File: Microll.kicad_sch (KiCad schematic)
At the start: 6 parts, among them J1 USB_C_Receptacle, U1 AP7173-FNG-7, U2 STM32G0B1CBU6, U3 ESP32-C3-WROOM-02-N4, U4 LSM6DSL

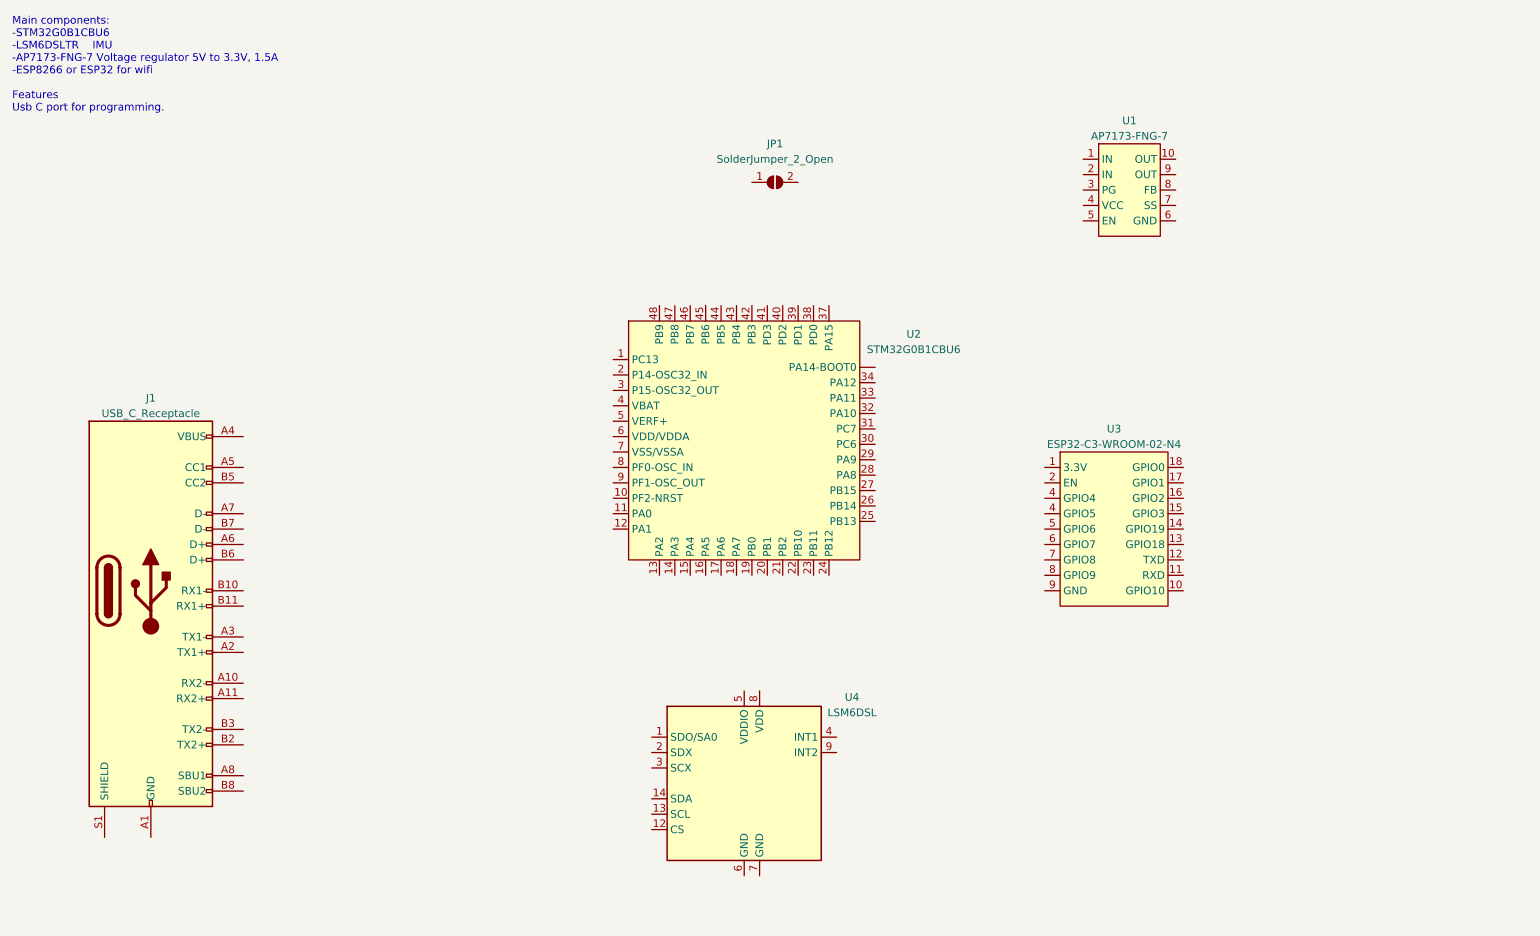
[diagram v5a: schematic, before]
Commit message: Added some notes on programming the STM32 and ESP32 over USB. Added datasheets to all components.
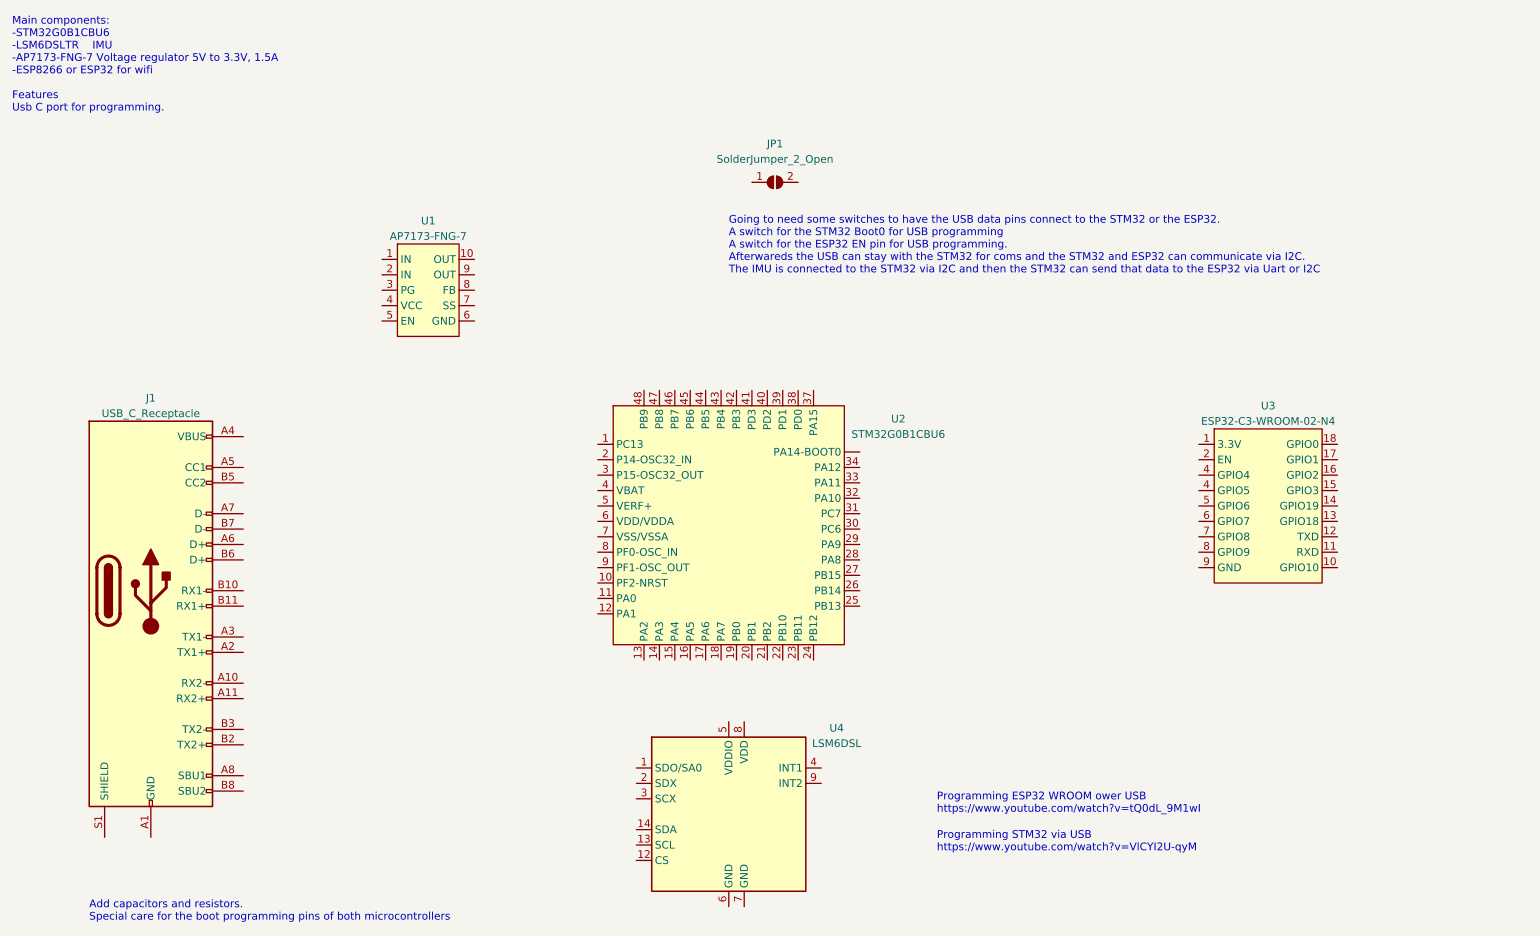
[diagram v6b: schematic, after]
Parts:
- J1: Datasheet2 (none) -> https://mm.digikey.com/Volume0/opasdata/d220001/medias/docu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
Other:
- note added: "Add capacitors and resistors. Special care for the boot programming pins of both microcontrollers"
- note added: "Going to need some switches to have the USB data pins connect to the STM32 or the ESP32. A switch for the STM32 Boot0 for USB programming A switch for the ESP32 EN pin for USB programming. Afterwareds the USB can stay with the STM32 for coms and the STM32 and ESP32 can communicate via I2C. The IMU is connected to the STM32 via I2C and then the STM32 can send that data to the ESP32 via Uart or I2C"
- note added: "Programming ESP32 WROOM ower USB https://www.youtube.com/watch?v=tQ0dL_9M1wI"
- note added: "Programming STM32 via USB https://www.youtube.com/watch?v=VlCYI2U-qyM"
- moved on the sheet: U1, U2, U3, U4
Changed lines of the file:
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@@
 (kicad_sch (version 20211123) (generator eeschema)
   (paper "A4")
+  (text "Going to need some switches to have the USB data pins connect to the STM32 or the ESP32.\nA switch for the STM32 Boot0 for USB programming\nA switch for the ESP32 EN pin for USB programming.\nAfterwareds the USB can stay with the STM32 for coms and the STM32 and ESP32 can communicate via I2C.\nThe IMU is connected to the STM32 via I2C and then the STM32 can send that data to the ESP32 via Uart or I2C"
+    (at 133.35 58.42 0)
+    (effects (font (size 1.27 1.27)) (justify left bottom))
+  )
+  (text "Programming ESP32 WROOM ower USB\nhttps://www.youtube.com/watch?v=tQ0dL_9M1wI"
+    (at 167.64 147.32 0)
+    (effects (font (size 1.27 1.27)) (justify left bottom))
+  )
+  (text "Programming STM32 via USB\nhttps://www.youtube.com/watch?v=VlCYI2U-qyM"
+    (at 167.64 153.67 0)
+    (effects (font (size 1.27 1.27)) (justify left bottom))
+  )
+  (text "Add capacitors and resistors.\nSpecial care for the boot programming pins of both microcontrollers"
+    (at 27.94 165.1 0)
+    (effects (font (size 1.27 1.27)) (justify left bottom))
+  )
   (text "Main components:\n-STM32G0B1CBU6	\n-LSM6DSLTR	IMU\n-AP7173-FNG-7 Voltage regulator 5V to 3.3V, 1.5A\n-ESP8266 or ESP32 for wifi\n\nFeatures\nUsb C port for programming."
     (at 15.24 31.75 0)
@@
     (pin "2")
   )
-  (symbol (lib_id "ESP32:ESP32-C3-WROOM-02-N4") (at 196.85 96.52 0) (unit 1)
+  (symbol (lib_id "ESP32:ESP32-C3-WROOM-02-N4") (at 222.25 92.71 0) (unit 1)
     (in_bom yes) (on_board yes)
-    (property "Reference" "U3" (id 0) (at 196.85 83.82 0))
-    (property "Value" "ESP32-C3-WROOM-02-N4" (id 1) (at 196.85 86.36 0))
-    (property "Footprint" "ESP32:ESP32-C3-WROOM-02-N4" (id 2) (at 196.85 96.52 0)
+    (property "Reference" "U3" (id 0) (at 222.25 80.01 0))
+    (property "Value" "ESP32-C3-WROOM-02-N4" (id 1) (at 222.25 82.55 0))
+    (property "Footprint" "ESP32:ESP32-C3-WROOM-02-N4" (id 2) (at 222.25 92.71 0)
       (effects (font (size 1.27 1.27)) hide)
     )
-    (property "Datasheet" "" (id 3) (at 196.85 96.52 0)
+    (property "Datasheet" "https://www.espressif.com/sites/default/files/documentation/esp32-c3-wroom-02_datasheet_en.pdf" (id 3) (at 222.25 92.71 0)
       (effects (font (size 1.27 1.27)) hide)
     )
@@
     (pin "9")
   )
-  (symbol (lib_id "STM32:STM32G0B1CBU6") (at 135.89 86.36 0) (unit 1)
+  (symbol (lib_id "STM32:STM32G0B1CBU6") (at 133.35 100.33 0) (unit 1)
     (in_bom yes) (on_board yes) (fields_autoplaced)
-    (property "Reference" "U2" (id 0) (at 163.83 68.1988 0))
-    (property "Value" "STM32G0B1CBU6" (id 1) (at 163.83 70.7388 0))
-    (property "Footprint" "STM32:STM32G0B1CBU6" (id 2) (at 128.27 77.47 0)
+    (property "Reference" "U2" (id 0) (at 161.29 82.1688 0))
+    (property "Value" "STM32G0B1CBU6" (id 1) (at 161.29 84.7088 0))
+    (property "Footprint" "STM32:STM32G0B1CBU6" (id 2) (at 125.73 91.44 0)
       (effects (font (size 1.27 1.27)) hide)
     )
-    (property "Datasheet" "" (id 3) (at 128.27 77.47 0)
+    (property "Datasheet" "file:///home/ruben/Downloads/stm32g0b1cb.pdf" (id 3) (at 125.73 91.44 0)
       (effects (font (size 1.27 1.27)) hide)
     )
@@
     (pin "9")
   )
-  (symbol (lib_id "AP7173-FNG-7:AP7173-FNG-7") (at 199.39 41.91 0) (unit 1)
+  (symbol (lib_id "AP7173-FNG-7:AP7173-FNG-7") (at 83.82 58.42 0) (unit 1)
     (in_bom yes) (on_board yes)
-    (property "Reference" "U1" (id 0) (at 199.39 33.02 0))
-    (property "Value" "AP7173-FNG-7" (id 1) (at 199.39 35.56 0))
-    (property "Footprint" "AP7173-FNG-7:AP7173-FNG-7" (id 2) (at 198.12 41.91 0)
+    (property "Reference" "U1" (id 0) (at 83.82 49.53 0))
+    (property "Value" "AP7173-FNG-7" (id 1) (at 83.82 52.07 0))
+    (property "Footprint" "AP7173-FNG-7:AP7173-FNG-7" (id 2) (at 82.55 58.42 0)
       (effects (font (size 1.27 1.27)) hide)
     )
-    (property "Datasheet" "" (id 3) (at 198.12 41.91 0)
+    (property "Datasheet" "https://www.diodes.com/assets/Datasheets/AP7173.pdf" (id 3) (at 82.55 58.42 0)
       (effects (font (size 1.27 1.27)) hide)
     )
@@
     (pin "9")
   )
-  (symbol (lib_id "Sensor_Motion:LSM6DSL") (at 135.89 142.24 0) (unit 1)
+  (symbol (lib_id "Sensor_Motion:LSM6DSL") (at 133.35 147.32 0) (unit 1)
     (in_bom yes) (on_board yes) (fields_autoplaced)
-    (property "Reference" "U4" (id 0) (at 153.67 128.0412 0))
-    (property "Value" "LSM6DSL" (id 1) (at 153.67 130.5812 0))
-    (property "Footprint" "Package_LGA:LGA-14_3x2.5mm_P0.5mm_LayoutBorder3x4y" (id 2) (at 125.73 160.02 0)
+    (property "Reference" "U4" (id 0) (at 151.13 133.1212 0))
+    (property "Value" "LSM6DSL" (id 1) (at 151.13 135.6612 0))
+    (property "Footprint" "Package_LGA:LGA-14_3x2.5mm_P0.5mm_LayoutBorder3x4y" (id 2) (at 123.19 165.1 0)
       (effects (font (size 1.27 1.27)) (justify left) hide)
     )
-    (property "Datasheet" "https://www.st.com/resource/en/datasheet/lsm6dsl.pdf" (id 3) (at 138.43 158.75 0)
+    (property "Datasheet" "https://www.st.com/resource/en/datasheet/lsm6dsl.pdf" (id 3) (at 135.89 163.83 0)
       (effects (font (size 1.27 1.27)) hide)
     )
@@
       (effects (font (size 1.27 1.27)) hide)
     )
+    (property "Datasheet2" "https://mm.digikey.com/Volume0/opasdata/d220001/medias/docus/5492/USB4105.pdf" (id 4) (at 38.1 110.49 0)
+      (effects (font (size 1.27 1.27)) hide)
+    )

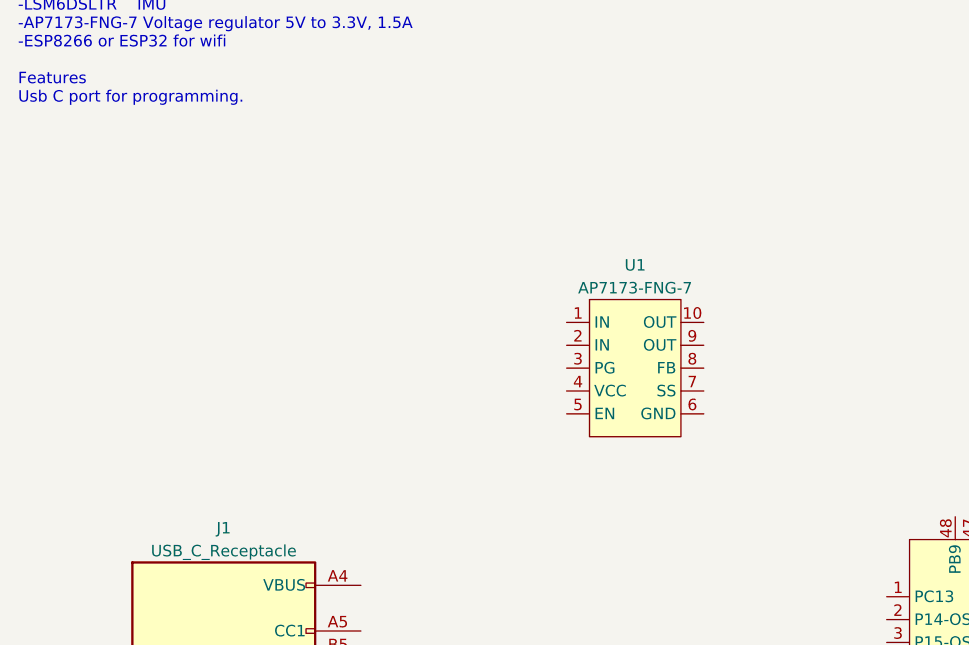
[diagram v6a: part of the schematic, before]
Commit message: Begun drafting linear regulator circuit and passive components
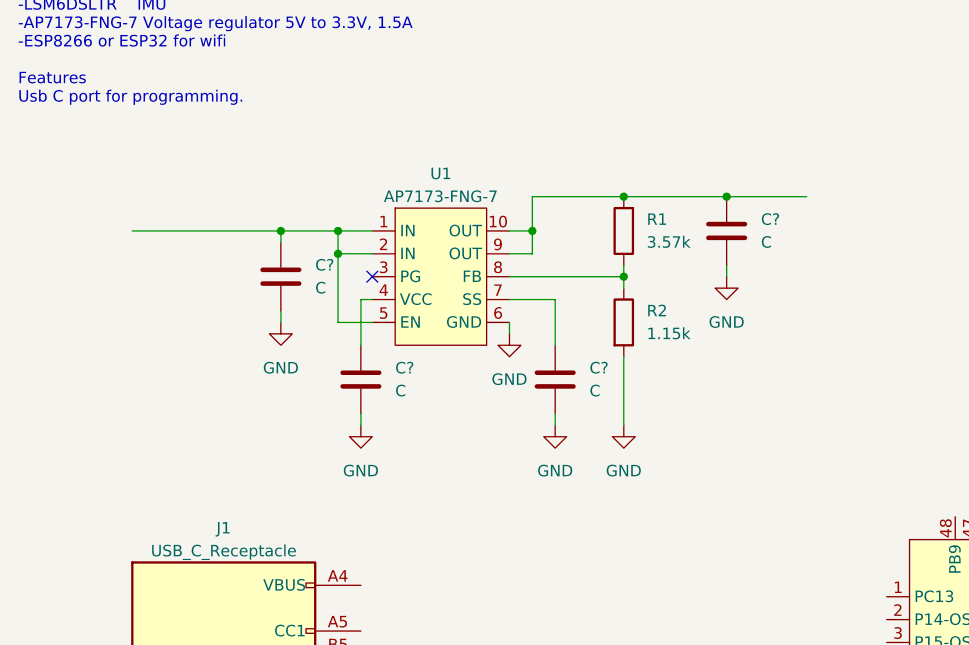
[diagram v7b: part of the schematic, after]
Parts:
- added C? (x4): C, symbol Device:C
- added R1: 3.57k, symbol Device:R
- added R2: 1.15k, symbol Device:R
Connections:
- net at U1.1 (IN): now also U1.2 (IN), U1.5 (EN), C?.1
- net at U1.10 (OUT): now also U1.9 (OUT), C?.1, R1.2
- net at U1.4 (VCC): now also C?.1
- net GND: now reaches U1.6 (GND)
- net GND: now also C?.2, C?.2, C?.2, C?.2, R2.2
- net at U1.7 (SS): now also C?.1
- net at U1.8 (FB): now also R1.1, R2.1
- no-connect marks 0 -> 1
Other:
- moved on the sheet: U1

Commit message: Thinking of swapping out linear regulator. Thinking about programming jumper to swap between microcontrollers
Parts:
- removed C?: C, symbol Device:C
- added JP? (x2): Jumper_2_Open, symbol Jumper:Jumper_2_Open
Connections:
- no-connect marks 1 -> 2
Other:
- note added: "Main components: -STM32G0B1CBU6 -LSM6DSLTR IMU -AP7173-FNG-7 Voltage regulator 5V to 3.3V, 1.5A. Second thoughts, look to swap to different regulator -ESP8266 or ESP32 for wifi Features Usb C port for programming."
- note removed: "Main components: -STM32G0B1CBU6 -LSM6DSLTR IMU -AP7173-FNG-7 Voltage regulator 5V to 3.3V, 1.5A -ESP8266 or ESP32 for wifi Features Usb C port for programming."
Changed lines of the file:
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@@
   )
   (no_connect (at 54.61 50.8))
+  (no_connect (at 69.85 53.34))
   (wire (pts (xy 50.8 45.72) (xy 50.8 48.26))
     (stroke (width 0) (type default) (color 0 0 0 0))
@@
     (stroke (width 0) (type default) (color 0 0 0 0))
   )
-  (wire (pts (xy 74.93 66.04) (xy 74.93 67.31))
-    (stroke (width 0) (type default) (color 0 0 0 0))
-  )
   (wire (pts (xy 72.39 41.91) (xy 72.39 45.72))
     (stroke (width 0) (type default) (color 0 0 0 0))
   )
-  (wire (pts (xy 69.85 53.34) (xy 74.93 53.34))
-    (stroke (width 0) (type default) (color 0 0 0 0))
-  )
   (wire (pts (xy 53.34 53.34) (xy 53.34 58.42))
     (stroke (width 0) (type default) (color 0 0 0 0))
@@
   )
   (wire (pts (xy 72.39 45.72) (xy 69.85 45.72))
-    (stroke (width 0) (type default) (color 0 0 0 0))
-  )
-  (wire (pts (xy 74.93 53.34) (xy 74.93 58.42))
     (stroke (width 0) (type default) (color 0 0 0 0))
   )
@@
     (effects (font (size 1.27 1.27)) (justify left bottom))
   )
-  (text "Main components:\n-STM32G0B1CBU6	\n-LSM6DSLTR	IMU\n-AP7173-FNG-7 Voltage regulator 5V to 3.3V, 1.5A\n-ESP8266 or ESP32 for wifi\n\nFeatures\nUsb C port for programming."
+  (text "Main components:\n-STM32G0B1CBU6	\n-LSM6DSLTR	IMU\n-AP7173-FNG-7 Voltage regulator 5V to 3.3V, 1.5A. Second thoughts, look to swap to different regulator\n-ESP8266 or ESP32 for wifi\n\nFeatures\nUsb C port for programming."
     (at 15.24 31.75 0)
     (effects (font (size 1.27 1.27)) (justify left bottom))
@@
     (pin "9")
   )
-  (symbol (lib_id "Device:C") (at 74.93 62.23 0) (unit 1)
-    (in_bom yes) (on_board yes) (fields_autoplaced)
-    (property "Reference" "C?" (id 0) (at 78.74 60.9599 0)
-      (effects (font (size 1.27 1.27)) (justify left))
-    )
-    (property "Value" "C" (id 1) (at 78.74 63.4999 0)
-      (effects (font (size 1.27 1.27)) (justify left))
-    )
-    (property "Footprint" "" (id 2) (at 75.8952 66.04 0)
-      (effects (font (size 1.27 1.27)) hide)
-    )
-    (property "Datasheet" "~" (id 3) (at 74.93 62.23 0)
+  (symbol (lib_id "Jumper:Jumper_2_Open") (at 186.69 34.29 0) (unit 1)
+    (in_bom yes) (on_board yes) (fields_autoplaced)
+    (property "Reference" "JP?" (id 0) (at 186.69 27.94 0))
+    (property "Value" "Jumper_2_Open" (id 1) (at 186.69 30.48 0))
+    (property "Footprint" "" (id 2) (at 186.69 34.29 0)
+      (effects (font (size 1.27 1.27)) hide)
+    )
+    (property "Datasheet" "~" (id 3) (at 186.69 34.29 0)
       (effects (font (size 1.27 1.27)) hide)
     )
@@
     (pin "S1")
   )
-  (symbol (lib_id "power:GND") (at 74.93 67.31 0) (unit 1)
-    (in_bom yes) (on_board yes) (fields_autoplaced)
-    (property "Reference" "#PWR?" (id 0) (at 74.93 73.66 0)
-      (effects (font (size 1.27 1.27)) hide)
-    )
-    (property "Value" "GND" (id 1) (at 74.93 72.39 0))
-    (property "Footprint" "" (id 2) (at 74.93 67.31 0)
-      (effects (font (size 1.27 1.27)) hide)
-    )
-    (property "Datasheet" "" (id 3) (at 74.93 67.31 0)
-      (effects (font (size 1.27 1.27)) hide)
-    )
-    (pin "1")
+  (symbol (lib_id "Jumper:Jumper_2_Open") (at 171.45 34.29 0) (unit 1)
+    (in_bom yes) (on_board yes) (fields_autoplaced)
+    (property "Reference" "JP?" (id 0) (at 171.45 27.94 0))
+    (property "Value" "Jumper_2_Open" (id 1) (at 171.45 30.48 0))
+    (property "Footprint" "" (id 2) (at 171.45 34.29 0)
+      (effects (font (size 1.27 1.27)) hide)
+    )
+    (property "Datasheet" "~" (id 3) (at 171.45 34.29 0)
+      (effects (font (size 1.27 1.27)) hide)
+    )
+    (pin "1")
+    (pin "2")
   )
   (symbol (lib_id "power:GND") (at 93.98 50.8 0) (unit 1)
@@
       (reference "#PWR?") (unit 1) (value "GND") (footprint "")
     )
-    (path "/ad2b2977-2533-45b4-9342-42db6f24df1a"
-      (reference "#PWR?") (unit 1) (value "GND") (footprint "")
-    )
     (path "/c62fb5ab-8d5a-4527-ab53-cd19bce67ac1"
       (reference "#PWR?") (unit 1) (value "GND") (footprint "")
@@
       (reference "C?") (unit 1) (value "C") (footprint "")
     )
-    (path "/556609bc-d75d-4026-ace8-31240684bd73"
-      (reference "C?") (unit 1) (value "C") (footprint "")
-    )
     (path "/8b6915cc-63b4-4776-bc52-9ec3dced6106"
       (reference "C?") (unit 1) (value "C") (footprint "")
@@
       (reference "JP1") (unit 1) (value "SolderJumper_2_Open") (footprint "SolderJumper-2_P1.3mm_Open_RoundedPad1.0x1.5mm")
     )
+    (path "/6b6deb6e-fdfe-4361-95f4-1e7797f44a14"
+      (reference "JP?") (unit 1) (value "Jumper_2_Open") (footprint "")
+    )
+    (path "/a0dcc4cb-c89a-44bf-bb33-a0edf7aa2fd4"
+      (reference "JP?") (unit 1) (value "Jumper_2_Open") (footprint "")
+    )
     (path "/4a2d5a3e-7463-47c6-9873-69f6c818af94"
